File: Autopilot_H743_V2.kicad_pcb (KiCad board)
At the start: 6 copper layers, 60 x 60 mm, 231 parts, among them J2 5V BEC INPUT PADS, J3 TYPE-C-31-M-12, J4 TF-01A / microSD, Q1 AO3401A, Q2 MMBT3906 PNP, Q3 MMBT2222A NPN, SW1 RESET, SW2 BOOT, U1 STM32H743VIT6, U10 BMI088, U11 MMC5983MA, U12 SPA06-003, U13 USBLC6-2SC6, U14 USBLC6-2SC6, U15 USBLC6-2SC6, U16 USBLC6-2SC6, U17 USBLC6-2SC6, U18 USBLC6-2SC6, U19 TPS2553DBVR, U2 AP63203WU-7, U20 USBLC6-2SC6, U21 SN74LV8T245PWR, U22 TMUX1574PWR, U23 TMUX1574PWR, U3 TPS2113APWR, U4 TPS7A2033PDBVR, U5 TUSB320LIRWBR, U6 TPS2553DBVR, U7 USBLC6-2SC6, U8 USBLC6-2SC6, U9 TPS7A2033PDBVR, Y1 8MHz

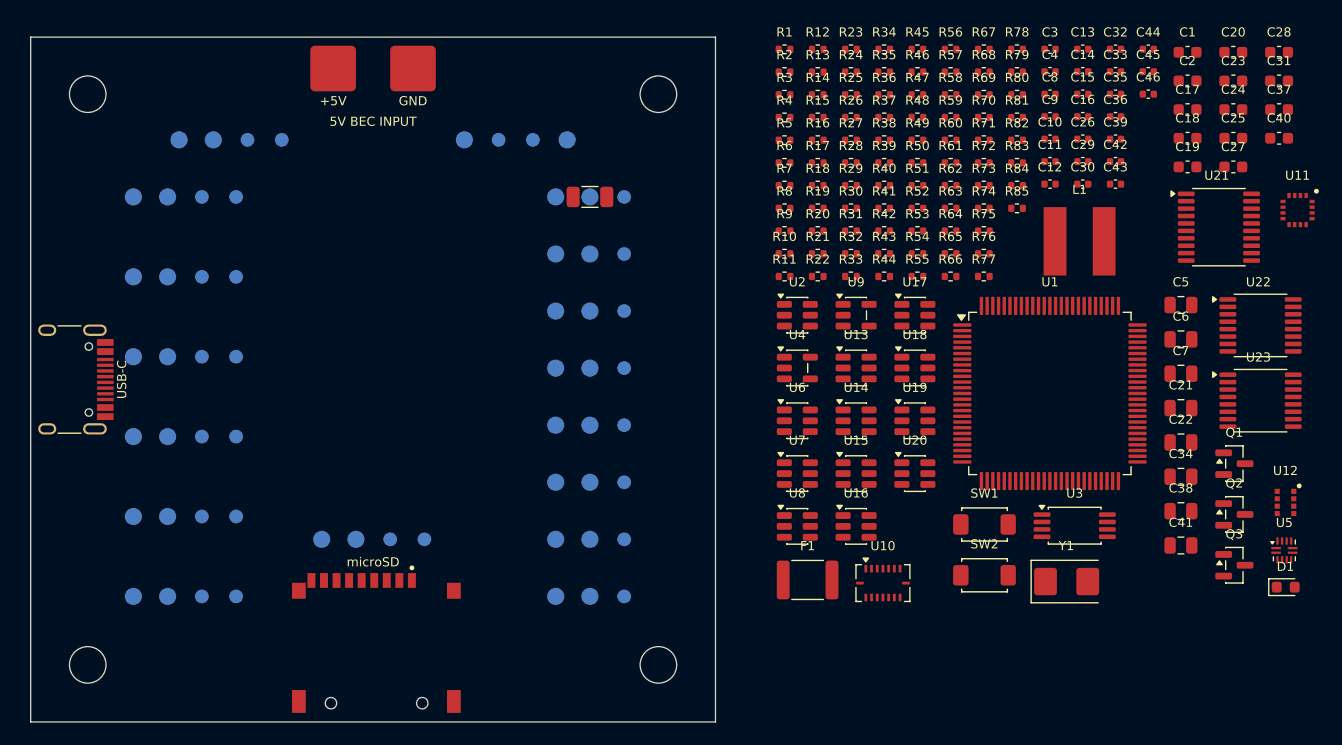
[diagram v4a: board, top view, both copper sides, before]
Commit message: Complete V2 routing; silkscreen cleanup remains
Finish the Quilter-routed board with the IMU chip-select connection, local MISO/gyro trace adjustments, the U21 power connection, and USB via clearance correction. Refill copper and align project rules with the selected fabrication budget.

Verification: 0 DRC errors, 0 unrouted connections, and 0 schematic parity issues. The remaining 201 warnings concern silkscreen and still need cleanup.

Replace the previous README images with one angled 3D render and keep the README to one line.
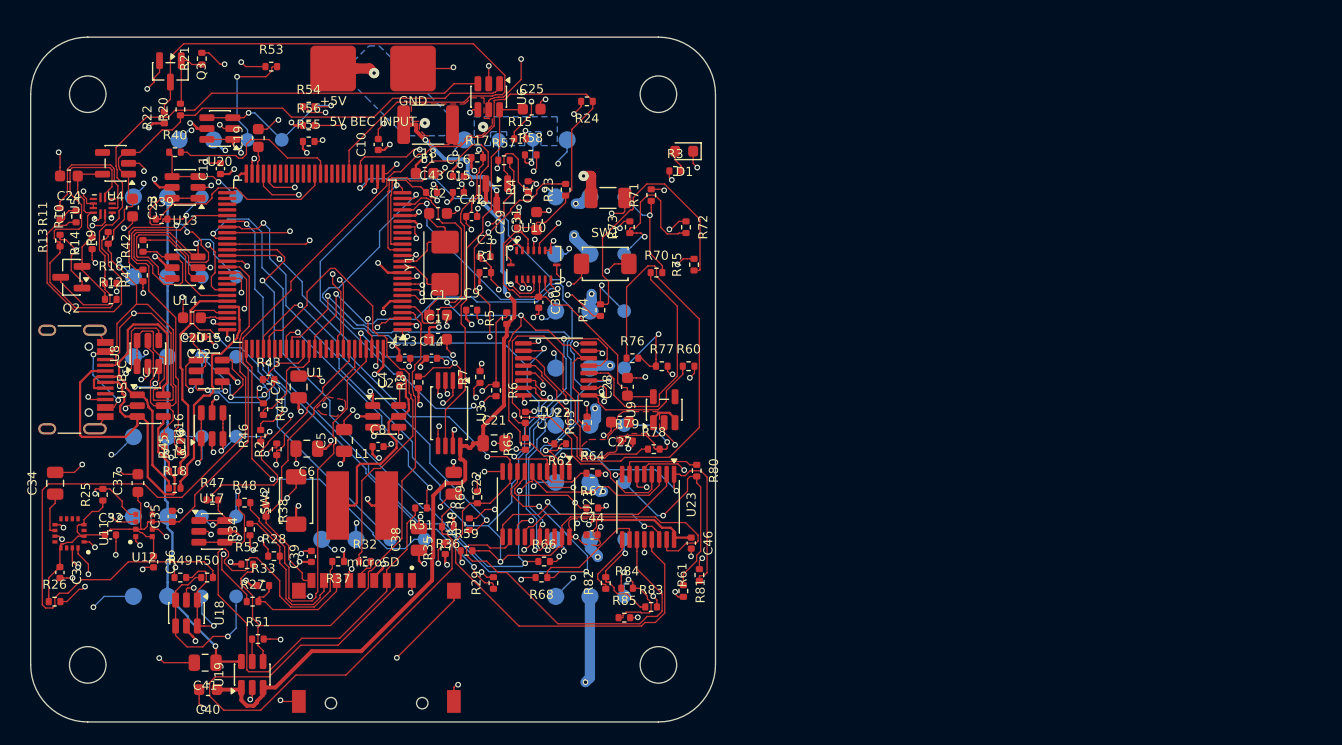
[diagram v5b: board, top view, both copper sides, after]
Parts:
- moved U11 111.3 mm to (93.4, 133.5), turned to -90 degrees
- moved U5 107.8 mm to (96.3, 104.8), turned to 90 degrees
- moved C40 105.5 mm to (105.5, 147.2), turned to 180 degrees
- moved C37 105.2 mm to (99.4, 129.1), turned to 90 degrees
- moved Q2 104.0 mm to (93.6, 111.0), turned to 180 degrees
- moved Q3 102.8 mm to (102.2, 93.0), turned to -90 degrees
- moved C33 102.4 mm to (92.6, 136.9), turned to -90 degrees
- moved C24 102.2 mm to (93.3, 102.2), turned to 180 degrees
- moved U12 100.0 mm to (99.9, 132.8), turned to 180 degrees
- moved C34 98.6 mm to (92.1, 129.1), turned to 90 degrees
- moved C32 97.8 mm to (97.0, 133.6)
- moved C23 97.1 mm to (98.9, 104.9), turned to -90 degrees
- moved C20 94.2 mm to (104.1, 114.6), turned to 180 degrees
- moved C36 92.9 mm to (100.8, 136.0), turned to -90 degrees
- moved C35 90.5 mm to (102.4, 132.0), turned to 90 degrees
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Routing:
- net /GND: track 0.00 -> 203.0 mm, vias 0 -> 132
- net /V3V3_SENS: track 0.00 -> 133.4 mm
- net /USB_VBUS: track 0.00 -> 88.5 mm, vias 0 -> 2
- net /ACTUATOR_OE_N: track 0.00 -> 87.4 mm, vias 0 -> 3
- net /PWM7_MCU: track 0.00 -> 78.1 mm, vias 0 -> 3
- net /PWM8_MCU: track 0.00 -> 73.7 mm, vias 0 -> 2
- net /V3V3_CORE: track 0.00 -> 72.3 mm, vias 0 -> 49
- net /PWM5_MCU: track 0.00 -> 72.2 mm, vias 0 -> 3
- net /OUT_BANK2_DSHOT: track 0.00 -> 69.1 mm, vias 0 -> 2
- net /PWM6_MCU: track 0.00 -> 66.9 mm, vias 0 -> 3
- net /V5_MAIN_PROT: track 0.00 -> 66.8 mm, vias 0 -> 2
- net /USART6_RX: track 0.00 -> 65.5 mm
- net /PWM4_MCU: track 0.00 -> 64.8 mm, vias 0 -> 5
- net /SD_D3_CARD: track 0.00 -> 61.5 mm, vias 0 -> 2
- net /PWM3_MCU: track 0.00 -> 56.6 mm, vias 0 -> 3
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- added copper zone on In1.Cu, net /GND
- added copper zone on In4.Cu, net /GND
- added copper zone on In3.Cu, net /V3V3_CORE
- added copper zone on B.Cu, net /V5_MAIN_IN
- added copper zone on F.Cu, net /V5_MAIN_IN
- added copper zone on In3.Cu, net /V5_MAIN_IN
- added copper zone on F.Cu, net /V5_SYS
- added copper zone on In3.Cu, net /V5_SYS
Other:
- outline, holes or cut-outs redrawn
- board text removed: "SERVO: BEC"
- board text removed: "UART: 5V"
- board text removed: "V2 / BOTTOM"
